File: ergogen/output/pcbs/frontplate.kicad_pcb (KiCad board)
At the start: 2 copper layers, 117.2 x 96.7 mm, 5 parts

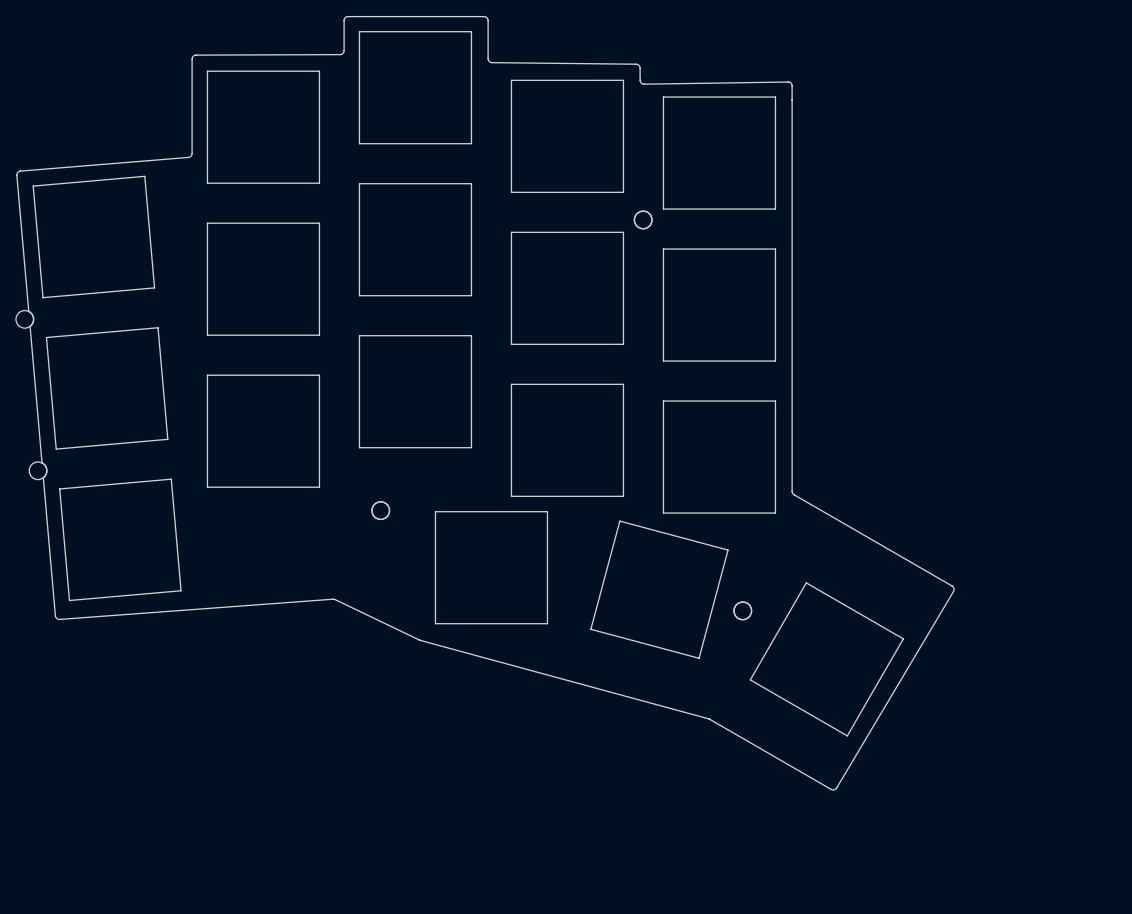
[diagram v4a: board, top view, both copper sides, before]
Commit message: Changed thumb splay
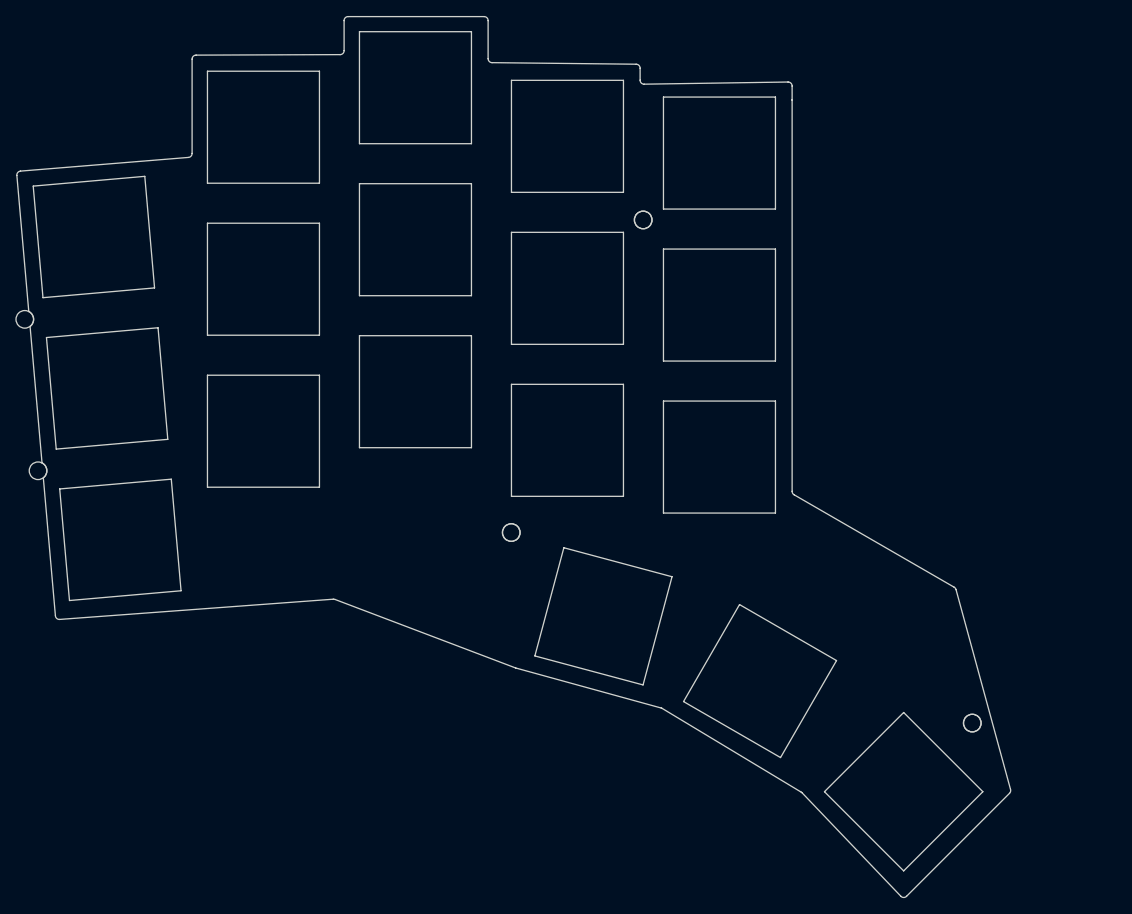
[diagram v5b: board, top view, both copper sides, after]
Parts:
- moved MH5 31.9 mm to (206.5, 122.9), turned to -45 degrees
- moved MH4 16.5 mm to (148.9, 99.1), turned to -15 degrees
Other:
- board size 117.2 x 96.7 mm -> 124.2 x 110.1 mm

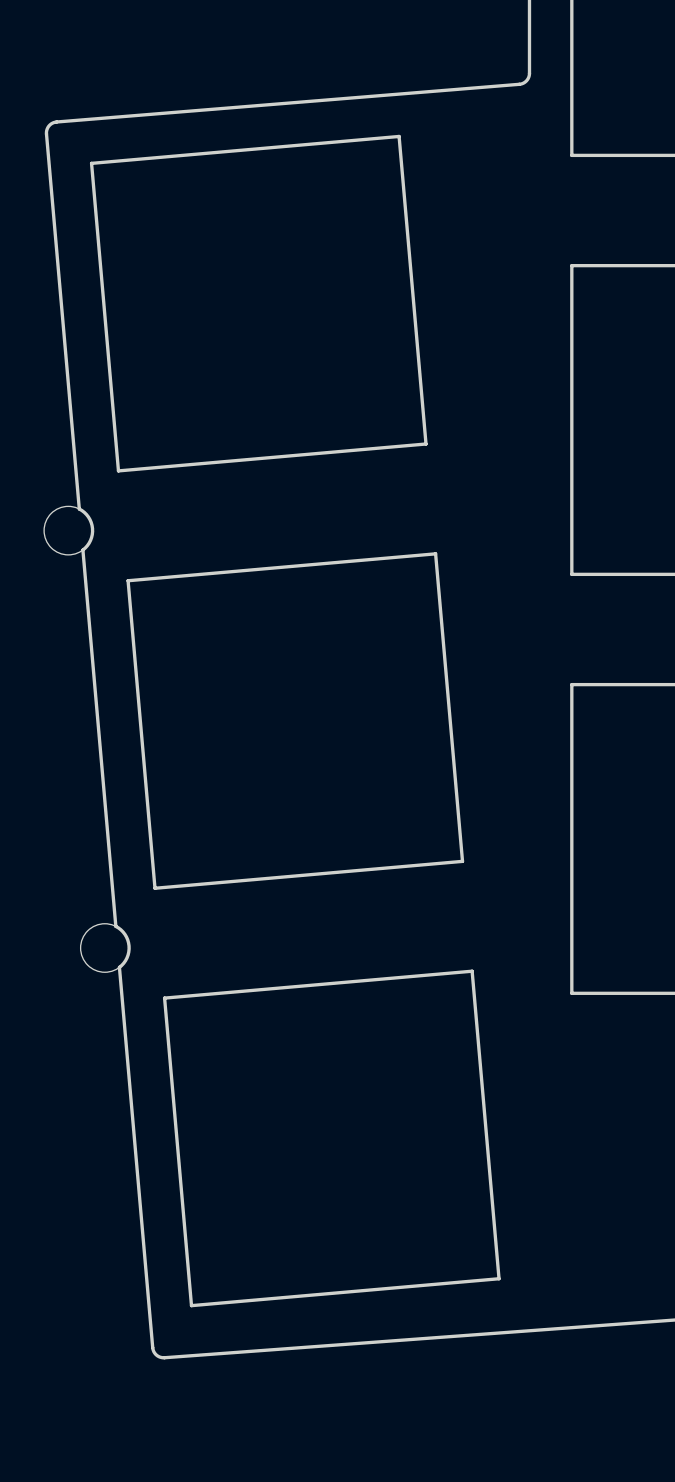
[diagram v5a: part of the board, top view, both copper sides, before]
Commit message: Moved screws back onto board
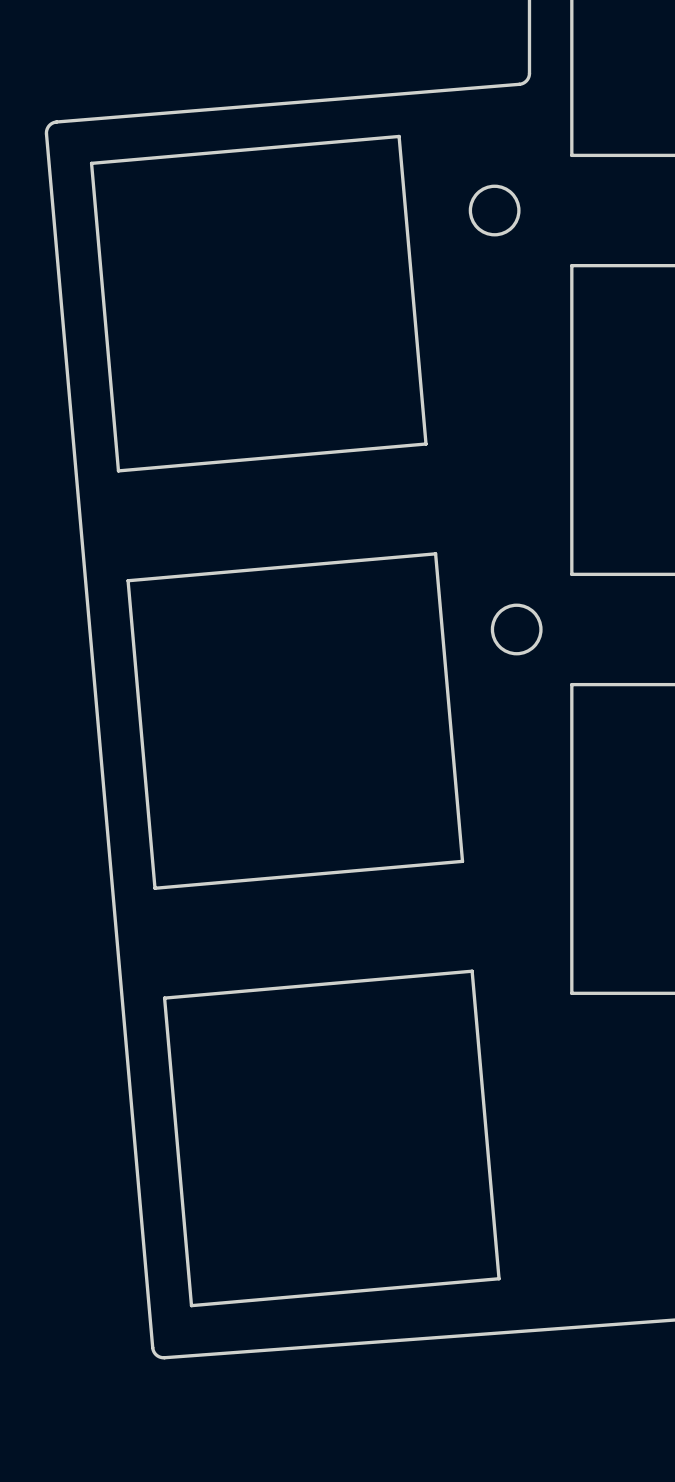
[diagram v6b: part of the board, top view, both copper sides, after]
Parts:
- moved MH1 24.2 mm to (107.4, 57.9), turned to 0 degrees
- moved MH2 23.6 mm to (108.4, 76.9), turned to 0 degrees
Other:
- outline, holes or cut-outs redrawn
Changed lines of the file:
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@@
   (net 0 "")
   (module "ceoloide:mounting_hole_npth" (layer F.Cu)
-      (at 88.05221169999999 72.4364306 5)
-      (fp_text reference "MH1" (at 0 2.55 5) (layer F.SilkS) hide (effects (font (size 1 1) (thickness 0.15))))
-      (pad "" np_thru_hole circle (at 0 0 5) (size 2.2 2.2) (drill 2.2) (layers *.Cu *.Mask))
+      (at 107.384445 57.919590400000004 0)
+      (fp_text reference "MH1" (at 0 2.55 0) (layer F.SilkS) hide (effects (font (size 1 1) (thickness 0.15))))
+      (pad "" np_thru_hole circle (at 0 0 0) (size 2.2 2.2) (drill 2.2) (layers *.Cu *.Mask))
   )
   (module "ceoloide:mounting_hole_npth" (layer F.Cu)
-      (at 89.70817079999999 91.3641299 5)
-      (fp_text reference "MH2" (at 0 2.55 5) (layer F.SilkS) hide (effects (font (size 1 1) (thickness 0.15))))
-      (pad "" np_thru_hole circle (at 0 0 5) (size 2.2 2.2) (drill 2.2) (layers *.Cu *.Mask))
+      (at 108.384445 76.9195904 0)
+      (fp_text reference "MH2" (at 0 2.55 0) (layer F.SilkS) hide (effects (font (size 1 1) (thickness 0.15))))
+      (pad "" np_thru_hole circle (at 0 0 0) (size 2.2 2.2) (drill 2.2) (layers *.Cu *.Mask))
   )
   (module "ceoloide:mounting_hole_npth" (layer F.Cu)
@@
       (pad "" np_thru_hole circle (at 0 0 -45) (size 2.2 2.2) (drill 2.2) (layers *.Cu *.Mask))
   )
-  (gr_line (start 91.87824460323029 109.49068746980254) (end 90.36871289999999 92.2437231) (layer Edge.Cuts) (stroke (width 0.15) (type default)))
-(gr_line (start 88.54919959999998 71.4551034) (end 87.06061104775414 54.447423555018986) (layer Edge.Cuts) (stroke (width 0.15) (type default)))
-(gr_line (start 90.2058682 90.38316239999999) (end 88.71211749999999 73.3165013) (layer Edge.Cuts) (stroke (width 0.15) (type default)))
+  (gr_line (start 91.87824460323029 109.49068746980254) (end 87.06061104775414 54.447423555018986) (layer Edge.Cuts) (stroke (width 0.15) (type default)))
 (gr_line (start 87.51811429808367 53.90547845906503) (end 108.50503754967045 52.19601094528491) (layer Edge.Cuts) (stroke (width 0.15) (type default)))
 (gr_line (start 108.964445 51.69766144933076) (end 108.964445 39.90788282277217) (layer Edge.Cuts) (stroke (width 0.15) (type default)))
@@
 (gr_line (start 207.8101585 131.4806626) (end 197.9106636 121.58116769999998) (layer Edge.Cuts) (stroke (width 0.15) (type default)))
 (gr_line (start 197.9106636 121.58116769999998) (end 188.01116869999998 131.4806626) (layer Edge.Cuts) (stroke (width 0.15) (type default)))
-(gr_arc (start 88.71211749999999 73.3165013) (mid 89.14802249999998 72.3405203) (end 88.54919959999998 71.4551034) (layer Edge.Cuts) (stroke (width 0.15) (type default)))
-(gr_arc (start 90.36871289999999 92.2437231) (mid 90.80398159999999 91.2682196) (end 90.2058682 90.3831623) (layer Edge.Cuts) (stroke (width 0.15) (type default)))
+(gr_circle (center 107.384445 57.919590400000004) (end 108.484445 57.919590400000004) (layer Edge.Cuts) (stroke (width 0.15) (type default)) (fill none))
+(gr_circle (center 108.384445 76.9195904) (end 109.484445 76.9195904) (layer Edge.Cuts) (stroke (width 0.15) (type default)) (fill none))
 (gr_circle (center 165.35244509999998 60.01059040000001) (end 166.45244509999998 60.01059040000001) (layer Edge.Cuts) (stroke (width 0.15) (type default)) (fill none))
 (gr_circle (center 148.8598077 99.0848776) (end 149.9598077 99.0848776) (layer Edge.Cuts) (stroke (width 0.15) (type default)) (fill none))

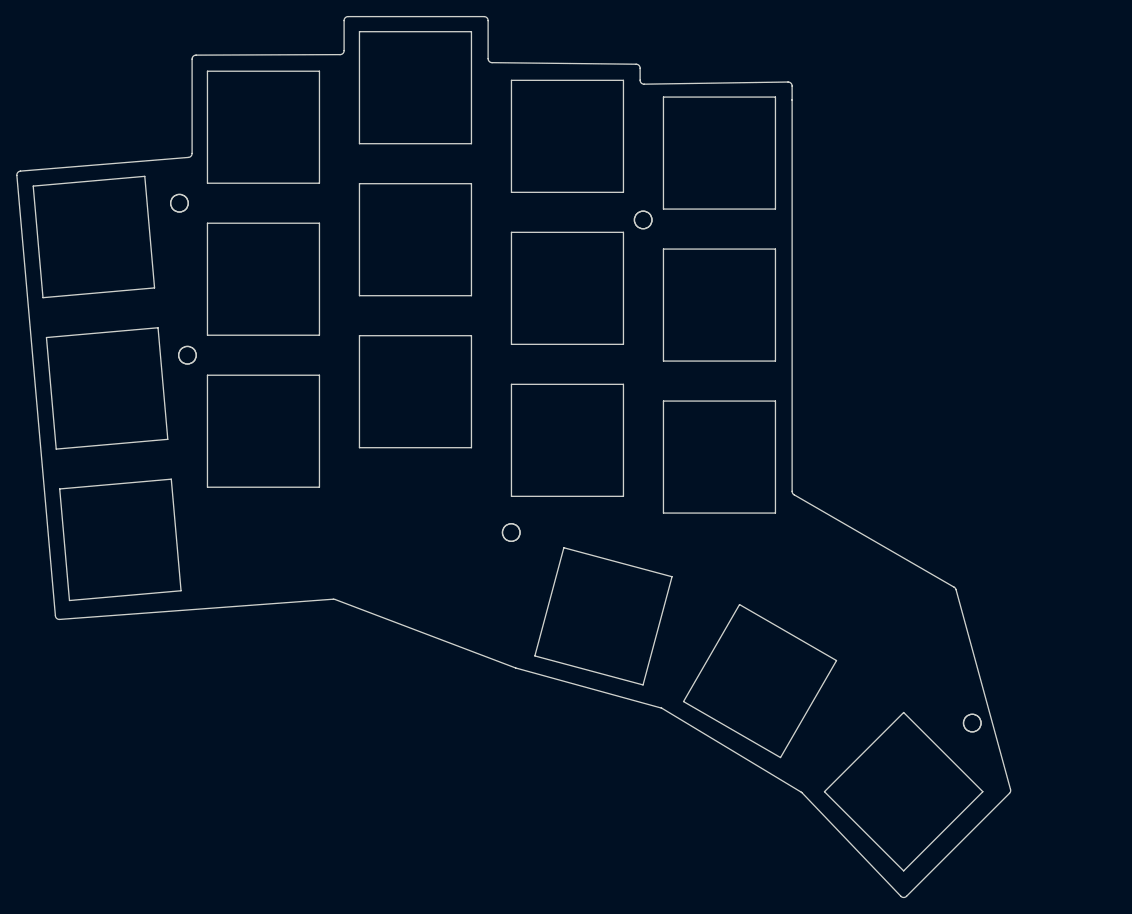
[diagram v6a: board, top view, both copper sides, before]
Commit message: Moved screws around a bit
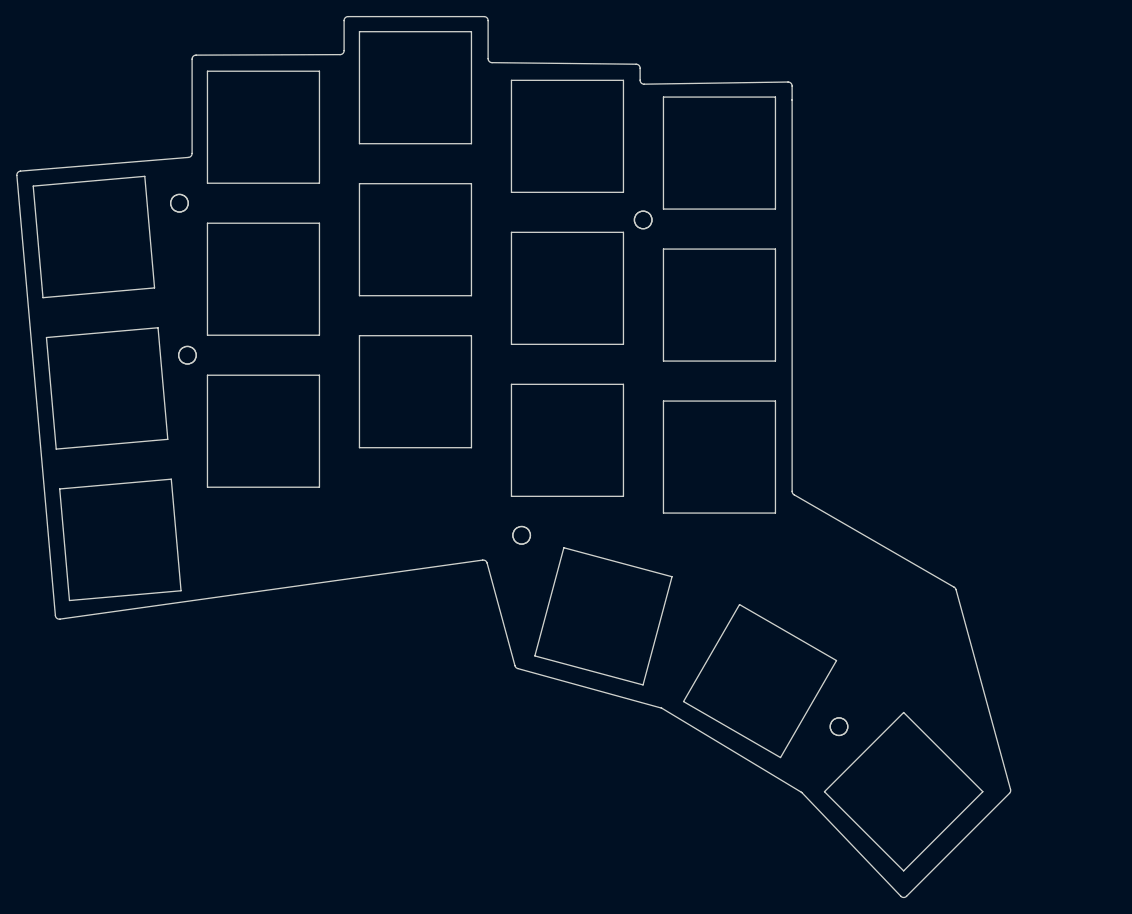
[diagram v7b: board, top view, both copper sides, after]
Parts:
- moved MH5 16.7 mm to (189.8, 123.4), turned to -30 degrees
- moved MH4 1.34 mm to (150.2, 99.4)
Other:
- outline, holes or cut-outs redrawn
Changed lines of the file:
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@@
   )
   (module "ceoloide:mounting_hole_npth" (layer F.Cu)
-      (at 148.8598077 99.0848776 -15)
+      (at 150.1570461 99.4324716 -15)
       (fp_text reference "MH4" (at 0 2.55 -15) (layer F.SilkS) hide (effects (font (size 1 1) (thickness 0.15))))
       (pad "" np_thru_hole circle (at 0 0 -15) (size 2.2 2.2) (drill 2.2) (layers *.Cu *.Mask))
   )
   (module "ceoloide:mounting_hole_npth" (layer F.Cu)
-      (at 206.488576 122.90275019999999 -45)
-      (fp_text reference "MH5" (at 0 2.55 -45) (layer F.SilkS) hide (effects (font (size 1 1) (thickness 0.15))))
-      (pad "" np_thru_hole circle (at 0 0 -45) (size 2.2 2.2) (drill 2.2) (layers *.Cu *.Mask))
+      (at 189.8298246 123.3510864 -30)
+      (fp_text reference "MH5" (at 0 2.55 -30) (layer F.SilkS) hide (effects (font (size 1 1) (thickness 0.15))))
+      (pad "" np_thru_hole circle (at 0 0 -30) (size 2.2 2.2) (drill 2.2) (layers *.Cu *.Mask))
   )
-  (gr_line (start 91.87824460323029 109.49068746980254) (end 87.06061104775414 54.447423555018986) (layer Edge.Cuts) (stroke (width 0.15) (type default)))
+  (gr_line (start 91.87535728883249 109.45769882370212) (end 87.06061104775414 54.447423555018986) (layer Edge.Cuts) (stroke (width 0.15) (type default)))
 (gr_line (start 87.51811429808367 53.90547845906503) (end 108.50503754967045 52.19601094528491) (layer Edge.Cuts) (stroke (width 0.15) (type default)))
 (gr_line (start 108.964445 51.69766144933076) (end 108.964445 39.90788282277217) (layer Edge.Cuts) (stroke (width 0.15) (type default)))
@@
 (gr_line (start 197.5573001306715 144.5456552181502) (end 185.2184018103768 131.6245719172887) (layer Edge.Cuts) (stroke (width 0.15) (type default)))
 (gr_line (start 185.11474537091743 131.54156036435938) (end 167.73632242747522 121.07577102297391) (layer Edge.Cuts) (stroke (width 0.15) (type default)))
-(gr_line (start 167.61101352447525 121.02201021014679) (end 149.42297909295323 116.01776895205687) (layer Edge.Cuts) (stroke (width 0.15) (type default)))
-(gr_line (start 149.37827902664569 116.003177061327) (end 126.82809141312292 107.44890800214452) (layer Edge.Cuts) (stroke (width 0.15) (type default)))
-(gr_line (start 126.61389341312291 107.4177619021445) (end 92.41319770323031 109.94573156980263) (layer Edge.Cuts) (stroke (width 0.15) (type default)))
+(gr_line (start 167.61101352447525 121.02201021014679) (end 149.67542832928424 116.0872276331902) (layer Edge.Cuts) (stroke (width 0.15) (type default)))
+(gr_line (start 149.32552987561743 115.73612318902917) (end 145.83984366392013 102.89472334271511) (layer Edge.Cuts) (stroke (width 0.15) (type default)))
+(gr_line (start 145.28816068340882 102.53050838832783) (end 92.4425969819845 109.90929922465821) (layer Edge.Cuts) (stroke (width 0.15) (type default)))
 (gr_arc (start 87.51811424775414 53.90547845501909) (mid 87.17664344775413 54.0812949550191) (end 87.06061104775414 54.4474235550191) (layer Edge.Cuts) (stroke (width 0.15) (type default)))
 (gr_arc (start 108.5050376 52.19601094933076) (mid 108.83207 52.03655944933076) (end 108.964445 51.69766144933076) (layer Edge.Cuts) (stroke (width 0.15) (type default)))
@@
 (gr_arc (start 185.21840173422504 131.62457194226215) (mid 185.16934173422504 131.57960944226215) (end 185.11474533422503 131.54156034226216) (layer Edge.Cuts) (stroke (width 0.15) (type default)))
 (gr_arc (start 167.7363223907828 121.07577100087666) (mid 167.6755091907828 121.04459890087666) (end 167.6110134907828 121.02201020087666) (layer Edge.Cuts) (stroke (width 0.15) (type default)))
-(gr_arc (start 149.37827902664569 116.003177061327) (mid 149.4004574266457 116.010998761327) (end 149.42297912664569 116.017768961327) (layer Edge.Cuts) (stroke (width 0.15) (type default)))
-(gr_arc (start 126.8280914131229 107.4489080021445) (mid 126.72269801312291 107.4216051021445) (end 126.61389341312291 107.4177619021445) (layer Edge.Cuts) (stroke (width 0.15) (type default)))
-(gr_arc (start 91.8782446032303 109.49068746980264) (mid 92.0523782032303 109.82794416980263) (end 92.4131977032303 109.94573156980263) (layer Edge.Cuts) (stroke (width 0.15) (type default)))
+(gr_arc (start 149.32552986297674 115.73612314246033) (mid 149.45390776297674 115.95808674246032) (end 149.67542826297674 116.08722764246032) (layer Edge.Cuts) (stroke (width 0.15) (type default)))
+(gr_arc (start 145.83984367656083 102.89472338928387) (mid 145.63278067656083 102.60843598928388) (end 145.28816067656084 102.53050828928387) (layer Edge.Cuts) (stroke (width 0.15) (type default)))
+(gr_arc (start 91.87535728883246 109.45769882370203) (mid 92.06202788883246 109.80527372370203) (end 92.44259698883246 109.90929922370204) (layer Edge.Cuts) (stroke (width 0.15) (type default)))
 (gr_line (start 93.6367273 107.5834531) (end 107.5834531 106.3632727) (layer Edge.Cuts) (stroke (width 0.15) (type default)))
 (gr_line (start 107.5834531 106.3632727) (end 106.3632727 92.4165469) (layer Edge.Cuts) (stroke (width 0.15) (type default)))
@@
 (gr_circle (center 108.384445 76.9195904) (end 109.484445 76.9195904) (layer Edge.Cuts) (stroke (width 0.15) (type default)) (fill none))
 (gr_circle (center 165.35244509999998 60.01059040000001) (end 166.45244509999998 60.01059040000001) (layer Edge.Cuts) (stroke (width 0.15) (type default)) (fill none))
-(gr_circle (center 148.8598077 99.0848776) (end 149.9598077 99.0848776) (layer Edge.Cuts) (stroke (width 0.15) (type default)) (fill none))
-(gr_circle (center 206.488576 122.90275019999999) (end 207.588576 122.90275019999999) (layer Edge.Cuts) (stroke (width 0.15) (type default)) (fill none))
+(gr_circle (center 150.1570461 99.4324716) (end 151.2570461 99.4324716) (layer Edge.Cuts) (stroke (width 0.15) (type default)) (fill none))
+(gr_circle (center 189.8298246 123.3510864) (end 190.9298246 123.3510864) (layer Edge.Cuts) (stroke (width 0.15) (type default)) (fill none))
 )
